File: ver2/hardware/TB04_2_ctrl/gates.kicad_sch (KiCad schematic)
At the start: 14 parts, among them U1501 74AHC04, U1503 74LS08, U1504 74HC00, U1505 74LS00, U1506 74LS32, U1507 74LS08, U1509 74LS10

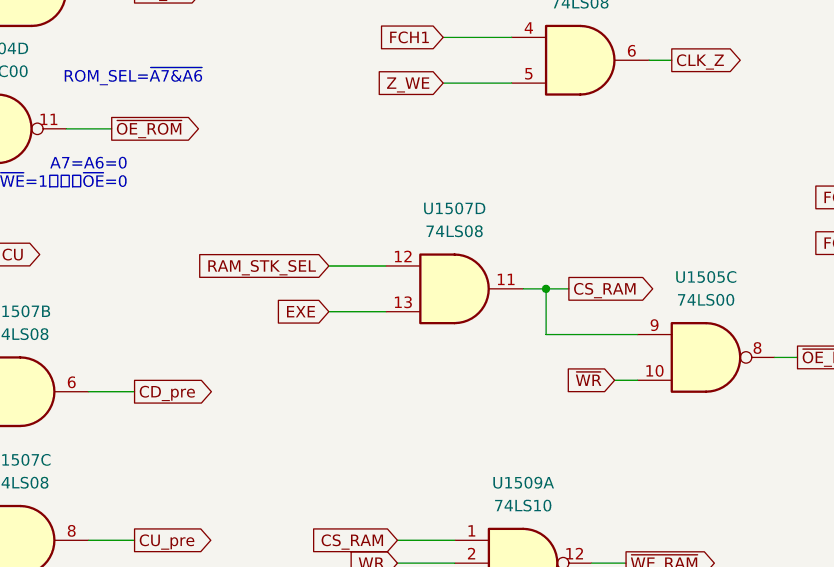
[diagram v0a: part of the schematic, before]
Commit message: ver2: 制御基板を分割完了・不要シートを整理(基板4分割の3枚目)
TB04_2_ctrl を分割完了。ai-reviewで検証し合格。
- 64信号すべてバスへ引き出し済み、ピン位置は確定表と完全一致
- 署名が変わったのは J101 のみ(USB-C→40ピンバスヘッダ)
- 電源入口は TB04_4_io のみ。他基板はバス1のVDD/GNDから受ける
- 各プロジェクトから未使用シートのファイルを削除

Co-Authored-By: Claude Opus 5 <noreply@anthropic.com>
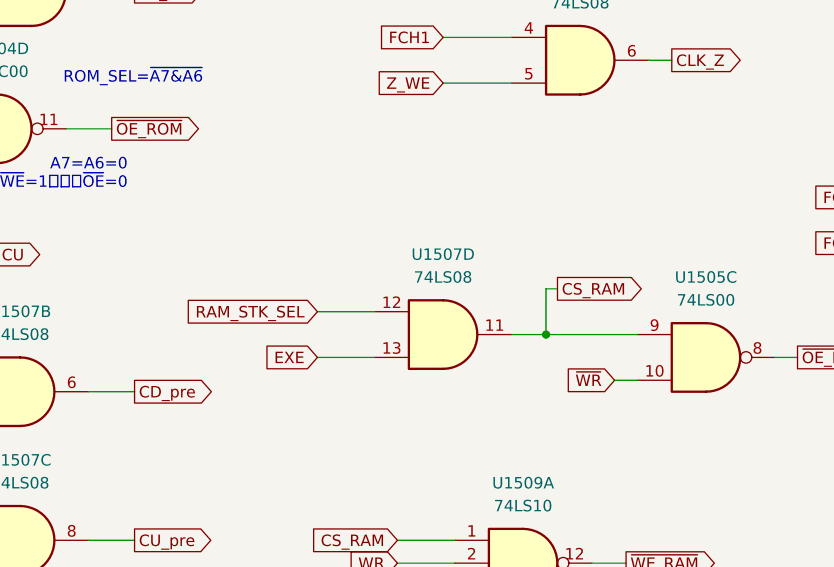
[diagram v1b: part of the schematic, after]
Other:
- moved on the sheet: U1507D
